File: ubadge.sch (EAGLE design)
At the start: 9 parts, among them IC1 ATTINY85

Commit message: fixed mislabled DM/DP (no board change)
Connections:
- net DM-TINY: now also IC1.PB3(ADC3), R1.2; no longer IC1.PB4(ADC2), R2.2
- net DP-TINY: now also IC1.PB4(ADC2), R2.2; no longer IC1.PB3(ADC3), R1.2
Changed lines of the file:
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@@
 </segment>
 </net>
-<net name="DP-TINY" class="0">
+<net name="DM-TINY" class="0">
 <segment>
 <pinref part="R1" gate="G$1" pin="2"/>
@@
 </segment>
 </net>
-<net name="DM-TINY" class="0">
+<net name="DP-TINY" class="0">
 <segment>
 <pinref part="R2" gate="G$1" pin="2"/>

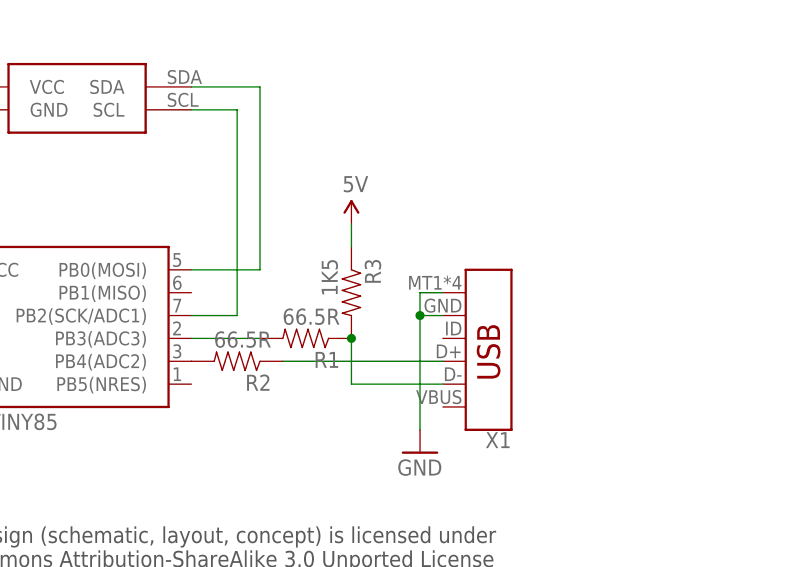
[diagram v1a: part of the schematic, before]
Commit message: swapped in usb connector with throughole alignment tabs and adjusted a few components. adding centroid, cam, and gerbv files.
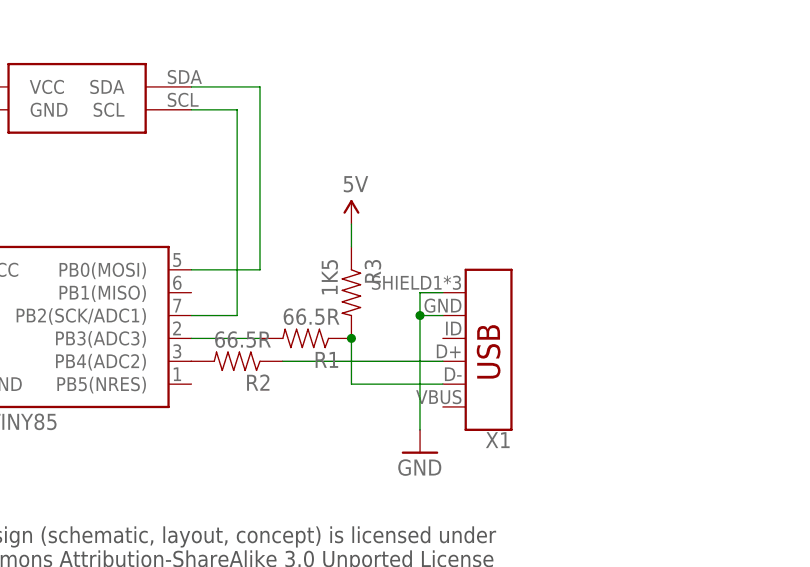
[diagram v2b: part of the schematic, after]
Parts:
- X1: device SparkFun-Connectors:USB_MICRO-B_SMT -> SparkFun-Connectors:USB_MICRO-B_FEMALE-SMT
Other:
- moved on the sheet: X1
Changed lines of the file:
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@@
 </classes>
 <parts>
-<part name="X1" library="SparkFun-Connectors" deviceset="USB_MICRO-B" device="_SMT"/>
+<part name="X1" library="SparkFun-Connectors" deviceset="USB_MICRO-B" device="_FEMALE-SMT"/>
 <part name="IC1" library="SparkFun" deviceset="ATTINY45" device="" value="ATTINY85"/>
 <part name="C1" library="SparkFun" deviceset="CAP" device="0402-CAP" value="0.1uf"/>
